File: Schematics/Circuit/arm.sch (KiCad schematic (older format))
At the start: 6 parts

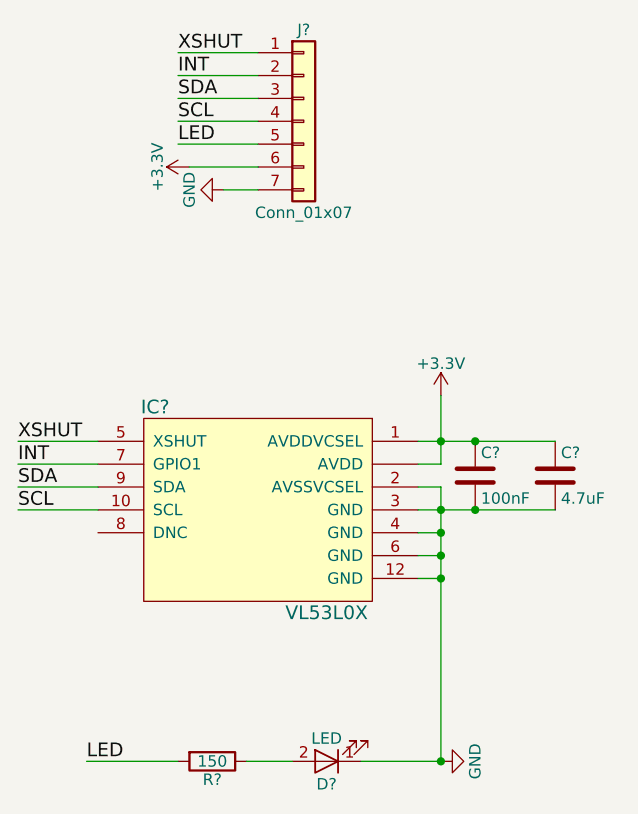
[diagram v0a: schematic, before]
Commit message: Edit finish circuits and some model work
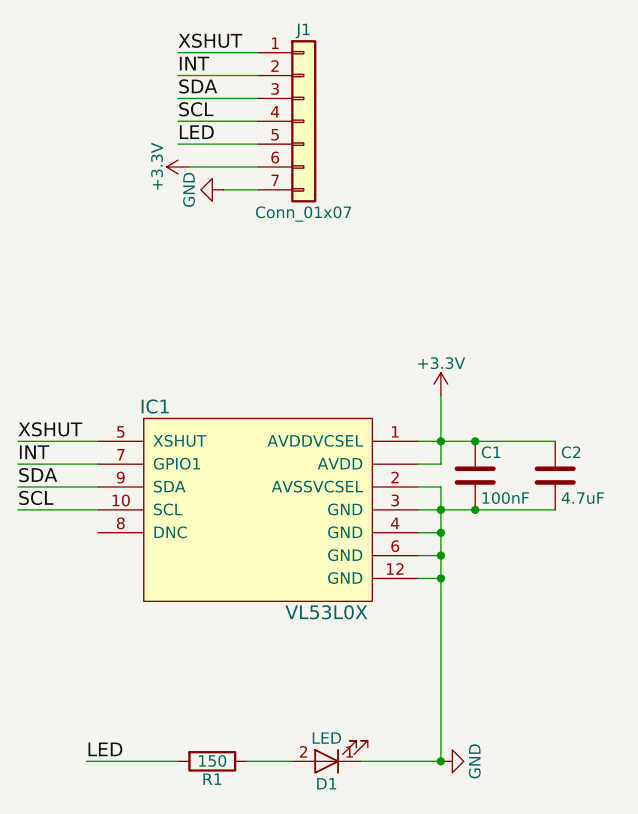
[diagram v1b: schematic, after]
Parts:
- C1: renamed from C?; footprint (none) -> Capacitors_SMD:C_0805
- C2: renamed from C?; footprint (none) -> Capacitors_SMD:C_0402
- D1: renamed from D?; footprint (none) -> Diodes_SMD:D_0603
- IC1: renamed from IC?; footprint (none) -> VL53L0X:XDCR_VL53L0CXV0DH%2f1
- J1: renamed from J?; footprint (none) -> CanSat:MOLEX_PicoBlade_7
- R1: renamed from R?; footprint (none) -> Resistors_SMD:R_0805
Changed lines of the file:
@@
 $EndDescr
 $Comp
-L VL53L0X IC?
+L VL53L0X IC1
 U 1 1 5A51D9B7
 P 6400 3000
-F 0 "IC?" H 5950 3450 60  0000 C CNN
+F 0 "IC1" H 5950 3450 60  0000 C CNN
 F 1 "VL53L0X" H 6700 2550 60  0000 C CNN
-F 2 "" H 6400 3000 60  0001 C CNN
+F 2 "VL53L0X:XDCR_VL53L0CXV0DH%2f1" H 6400 3000 60  0001 C CNN
 F 3 "" H 6400 3000 60  0001 C CNN
 	1    6400 3000
@@
 $EndComp
 $Comp
-L LED D?
+L LED D1
 U 1 1 5A51DA01
 P 6700 4100
-F 0 "D?" H 6700 4200 50  0000 C CNN
+F 0 "D1" H 6700 4200 50  0000 C CNN
 F 1 "LED" H 6700 4000 50  0000 C CNN
-F 2 "" H 6700 4100 50  0001 C CNN
+F 2 "Diodes_SMD:D_0603" H 6700 4100 50  0001 C CNN
 F 3 "" H 6700 4100 50  0001 C CNN
 	1    6700 4100
@@
 $EndComp
 $Comp
-L R R?
+L R R1
 U 1 1 5A51E094
 P 6200 4100
-F 0 "R?" V 6280 4100 50  0000 C CNN
+F 0 "R1" V 6280 4100 50  0000 C CNN
 F 1 "150" V 6200 4100 50  0000 C CNN
-F 2 "" V 6130 4100 50  0001 C CNN
+F 2 "Resistors_SMD:R_0805" V 6130 4100 50  0001 C CNN
 F 3 "" H 6200 4100 50  0001 C CNN
 	1    6200 4100
@@
 LED
 $Comp
-L GND #PWR?
+L GND #PWR01
 U 1 1 5A51E11C
 P 7200 4100
-F 0 "#PWR?" H 7200 3850 50  0001 C CNN
+F 0 "#PWR01" H 7200 3850 50  0001 C CNN
 F 1 "GND" H 7200 3950 50  0000 C CNN
 F 2 "" H 7200 4100 50  0001 C CNN
@@
 Connection ~ 7200 3000
 $Comp
-L C C?
+L C C1
 U 1 1 5A51E2B0
 P 7350 2850
-F 0 "C?" H 7375 2950 50  0000 L CNN
+F 0 "C1" H 7375 2950 50  0000 L CNN
 F 1 "100nF" H 7375 2750 50  0000 L CNN
-F 2 "" H 7388 2700 50  0001 C CNN
+F 2 "Capacitors_SMD:C_0805" H 7388 2700 50  0001 C CNN
 F 3 "" H 7350 2850 50  0001 C CNN
 	1    7350 2850
@@
 $EndComp
 $Comp
-L C C?
+L C C2
 U 1 1 5A51E305
 P 7700 2850
-F 0 "C?" H 7725 2950 50  0000 L CNN
+F 0 "C2" H 7725 2950 50  0000 L CNN
 F 1 "4.7uF" H 7725 2750 50  0000 L CNN
-F 2 "" H 7738 2700 50  0001 C CNN
+F 2 "Capacitors_SMD:C_0402" H 7738 2700 50  0001 C CNN
 F 3 "" H 7700 2850 50  0001 C CNN
 	1    7700 2850
@@
 SCL
 $Comp
-L +3.3V #PWR?
+L +3.3V #PWR02
 U 1 1 5A51E5A5
 P 7200 2500
-F 0 "#PWR?" H 7200 2350 50  0001 C CNN
+F 0 "#PWR02" H 7200 2350 50  0001 C CNN
 F 1 "+3.3V" H 7200 2640 50  0000 C CNN
 F 2 "" H 7200 2500 50  0001 C CNN
@@
 $EndComp
 $Comp
-L Conn_01x07 J?
+L Conn_01x07 J1
 U 1 1 5A51E5E2
 P 6600 1300
-F 0 "J?" H 6600 1700 50  0000 C CNN
+F 0 "J1" H 6600 1700 50  0000 C CNN
 F 1 "Conn_01x07" H 6600 900 50  0000 C CNN
-F 2 "" H 6600 1300 50  0001 C CNN
+F 2 "CanSat:MOLEX_PicoBlade_7" H 6600 1300 50  0001 C CNN
 F 3 "" H 6600 1300 50  0001 C CNN
 	1    6600 1300
@@
 LED
 $Comp
-L +3.3V #PWR?
+L +3.3V #PWR03
 U 1 1 5A51E6B2
 P 6100 1500
-F 0 "#PWR?" H 6100 1350 50  0001 C CNN
+F 0 "#PWR03" H 6100 1350 50  0001 C CNN
 F 1 "+3.3V" H 6100 1640 50  0000 C CNN
 F 2 "" H 6100 1500 50  0001 C CNN
@@
 $EndComp
 $Comp
-L GND #PWR?
+L GND #PWR04
 U 1 1 5A51E6D5
 P 6250 1600
-F 0 "#PWR?" H 6250 1350 50  0001 C CNN
+F 0 "#PWR04" H 6250 1350 50  0001 C CNN
 F 1 "GND" H 6250 1450 50  0000 C CNN
 F 2 "" H 6250 1600 50  0001 C CNN
